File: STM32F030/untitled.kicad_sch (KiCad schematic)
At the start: 7 parts, among them J2 Lin_Pots_connectors, J3 Optional Power and GND, J4 I2C, J5 SWD, J6 SPI, J7 UART, J8 MCP2200 GPIO

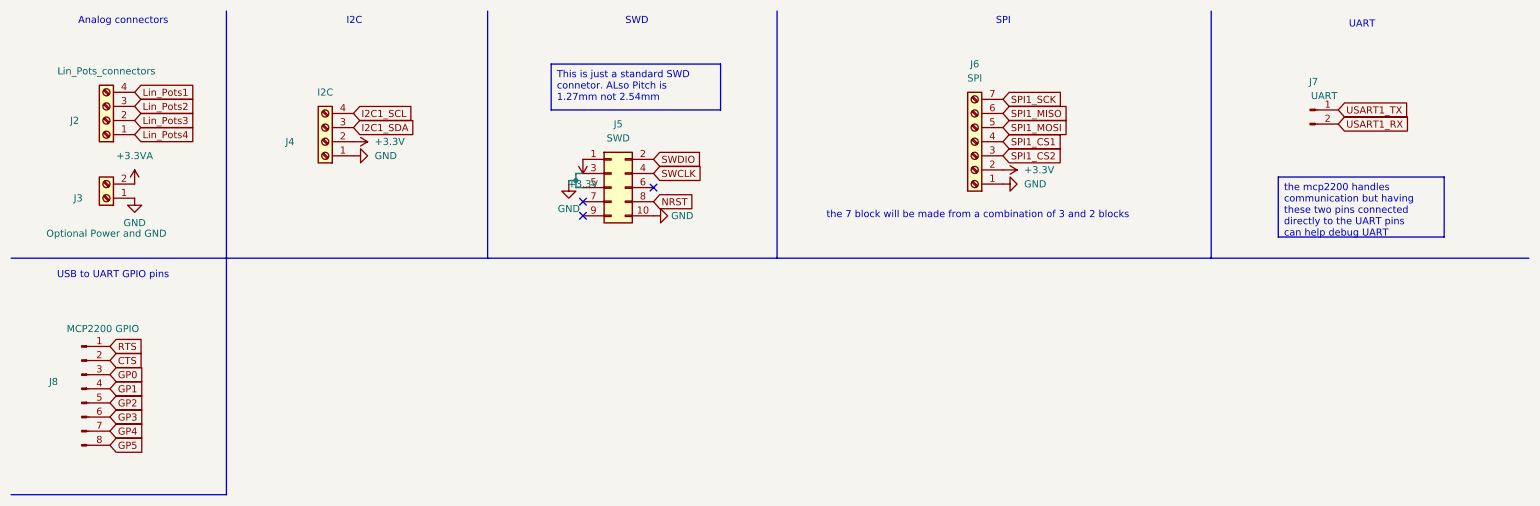
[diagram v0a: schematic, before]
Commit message: finished the schematic and most of the PCB just need the PWR planes and routes
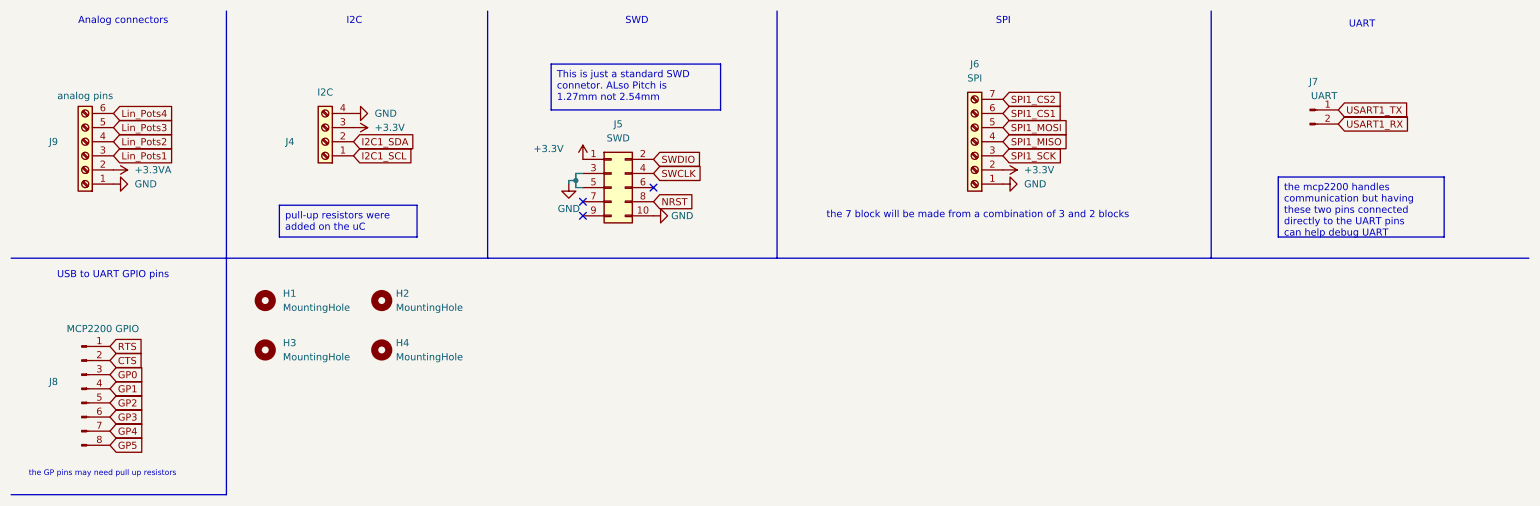
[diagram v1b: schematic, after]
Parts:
- removed J2: Lin_Pots_connectors, TerminalBlock_Phoenix:TerminalBlock_Phoenix_MKDS-1,5-4_1x04_P5.00mm_Horizontal, symbol Connector:Screw_Terminal_01x04
- removed J3: Optional Power and GND, TerminalBlock_Phoenix:TerminalBlock_Phoenix_MKDS-1,5-2_1x02_P5.00mm_Horizontal, symbol Connector:Screw_Terminal_01x02
- added H1, H2, H3, H4: MountingHole, MountingHole:MountingHole_3.2mm_M3_Pad_Via, symbol Mechanical:MountingHole
- added J9: analog pins, TerminalBlock_Phoenix:TerminalBlock_Phoenix_MKDS-1,5-6_1x06_P5.00mm_Horizontal, symbol Connector:Screw_Terminal_01x06
- J6: footprint TerminalBlock_Phoenix:TerminalBlock_Phoenix_PT-1,5-7-5.0-H_1x07_P5.00mm_Horizontal -> TerminalBlock_Phoenix:TerminalBlock_Phoenix_MKDS-1,5-7_1x07_P5.00mm_Horizontal
- J8: footprint (none) -> Connector_PinHeader_2.54mm:PinHeader_1x08_P2.54mm_Vertical
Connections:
- net +3.3V: now also J4.3 (Pin_3); no longer J4.2 (Pin_2)
- net +3.3VA: now also J9.2 (Pin_2)
- net GND: now also J4.4 (Pin_4), J9.1 (Pin_1); no longer J4.1 (Pin_1)
- net I2C1_SCL: now also J4.1 (Pin_1); no longer J4.4 (Pin_4)
- net I2C1_SDA: now also J4.2 (Pin_2); no longer J4.3 (Pin_3)
- net Lin_Pots1: now also J9.3 (Pin_3)
- net Lin_Pots2: now also J9.4 (Pin_4)
- net Lin_Pots3: now also J9.5 (Pin_5)
- net Lin_Pots4: now also J9.6 (Pin_6)
- net SPI1_CS1: now also J6.6 (Pin_6); no longer J6.4 (Pin_4)
- net SPI1_CS2: now also J6.7 (Pin_7); no longer J6.3 (Pin_3)
- net SPI1_MISO: now also J6.4 (Pin_4); no longer J6.6 (Pin_6)
- net SPI1_SCK: now also J6.3 (Pin_3); no longer J6.7 (Pin_7)
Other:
- note added: "the GP pins may need pull up resistors"
